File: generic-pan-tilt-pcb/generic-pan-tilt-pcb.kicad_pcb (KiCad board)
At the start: 2 copper layers, 104 x 57 mm, 86 parts, among them J1 B4P-VH-FB-B, J10 USB4115-03-C, J11 Conn_01x08, J12 Conn_01x08, J13 Conn_01x05, J2 NC5MAV, J3 NC5FAV, J5 BM03B-SRSS-TB, J7 BM03B-SRSS-TB, J8 B12B-PH-SM4-TB, J9 B12B-PH-SM4-TB, SW1 PTS 647 SK70 SMTR2 LFS, SW2 PTS 647 SK70 SMTR2 LFS, SW3 219-12LPST, U1 RP2040, U2 W25Q128JVS, U3 AP63203WU, U4 ISO1450DW, U5 MCP23017_SO, U6 LIS3DH, Y1 ABM8-272-T3

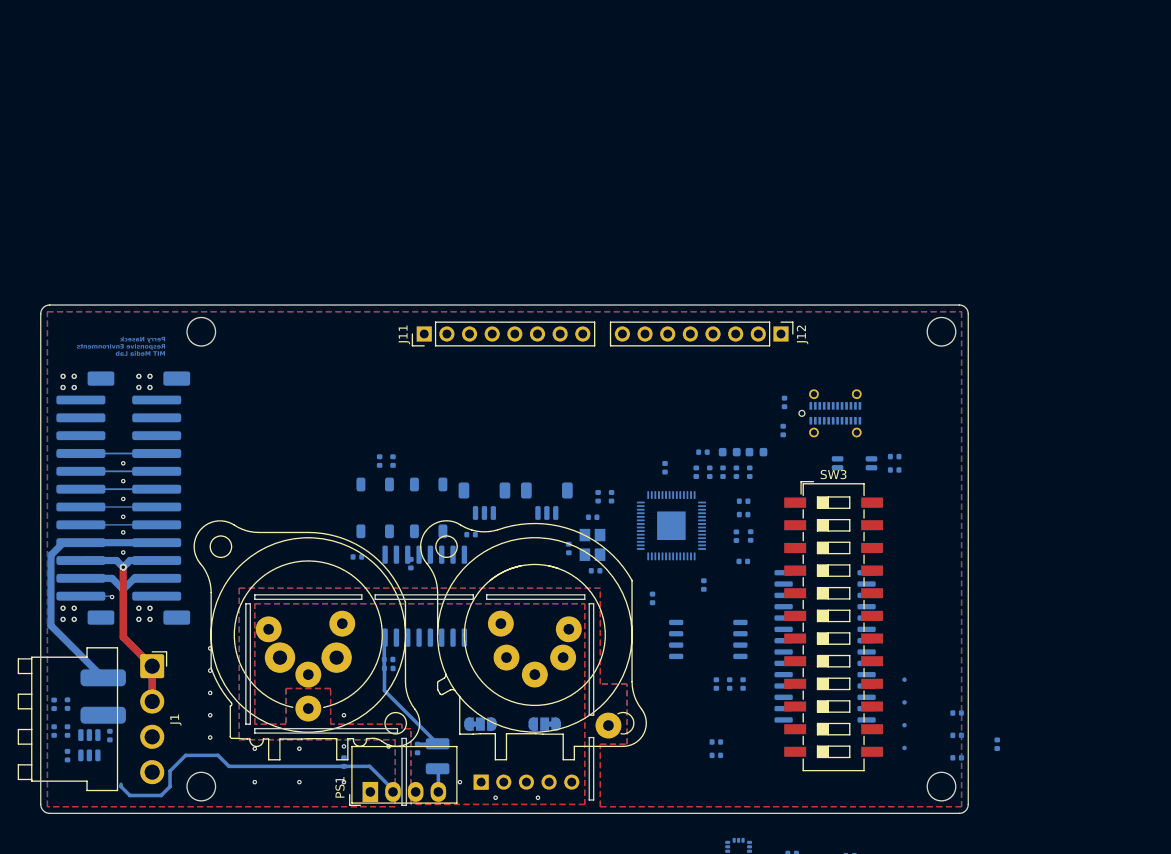
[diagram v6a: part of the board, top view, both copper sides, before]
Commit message: transplant hardware guide rp2040
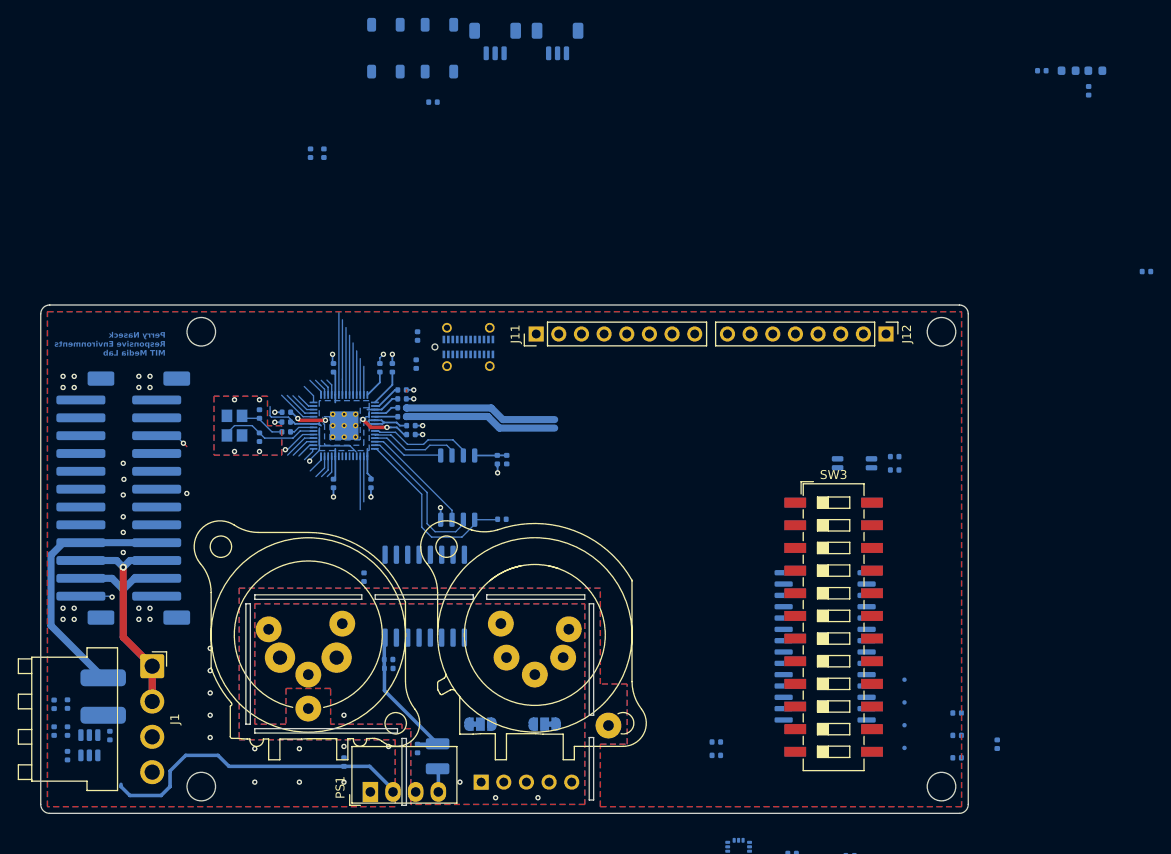
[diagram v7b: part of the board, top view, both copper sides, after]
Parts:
- removed C11: 0.1µF 10V, Capacitor_SMD:C_0402_1005Metric
- J5, J7: value BM03B-SRSS-TB -> BM03B-SRSS-TBT
- J8, J9: value B12B-PH-SM4-TB -> B12B-PH-SM4-TBT
- moved R8 81.3 mm to (205.0, 62.8)
- moved D1 57.2 mm to (196.2, 40.2)
- moved D2 57.2 mm to (199.2, 40.2)
- moved R1 57.2 mm to (193.2, 40.2)
- moved R3 57.2 mm to (198.5, 42.5)
- moved C5 53.9 mm to (108.5, 78.5), turned to 180 degrees
- moved R2 51.7 mm to (125.0, 43.8)
- moved J5 51.6 mm to (138.9, 37.0)
- moved J7 51.6 mm to (131.9, 37.0)
- moved SW1 51.6 mm to (119.7, 37.7)
- moved SW2 51.6 mm to (125.7, 37.7)
- moved Y1 42.3 mm to (102.7, 80.0)
- moved J10 41.8 mm to (128.9, 71.2)
- moved R5 41.8 mm to (123.1, 73.1)
- moved R4 41.8 mm to (123.2, 70.0)
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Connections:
- Y1 pad 1: GND -> /generic-pan-tilt-pcb_rp2040/XIN
- Y1 pad 2: /generic-pan-tilt-pcb_rp2040/XOUT_R -> GND
- Y1 pad 3: GND -> /generic-pan-tilt-pcb_rp2040/XOUT_R
- Y1 pad 4: /generic-pan-tilt-pcb_rp2040/XIN -> GND
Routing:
- net +3V3: track 66.5 -> 105.7 mm
- net /BOOTSEL: track 0.00 -> 21.2 mm
- net /USB_D-: track 0.00 -> 17.2 mm
- net /USB_D+: track 0.00 -> 17.2 mm
- net +1V1: track 0.00 -> 17.0 mm, vias 0 -> 4
- net /generic-pan-tilt-pcb_rp2040/QSPI_SD1: track 0.00 -> 16.8 mm
- net GND: track 3.54 -> 20.3 mm, vias 35 -> 53
- net /generic-pan-tilt-pcb_rp2040/QSPI_SD2: track 0.00 -> 12.9 mm
- net /generic-pan-tilt-pcb_rp2040/QSPI_SD3: track 0.00 -> 11.8 mm
- net /generic-pan-tilt-pcb_rp2040/XIN: track 0.00 -> 11.2 mm
- net /EXP_IRQ0: track 0.00 -> 10.5 mm, vias 0 -> 1
- net /generic-pan-tilt-pcb_rp2040/QSPI_CLK: track 0.00 -> 10.4 mm
- net /SPI_MOT_CS_MOT0_GPIO: track 0.00 -> 9.33 mm
- net /I2C_MOT_SDA: track 8.50 -> 0.00 mm
- net /I2C_MOT_SCL: track 8.50 -> 0.00 mm
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- added copper zone on B.Cu, net +1V1
- added copper zone on B.Cu, net +3V3

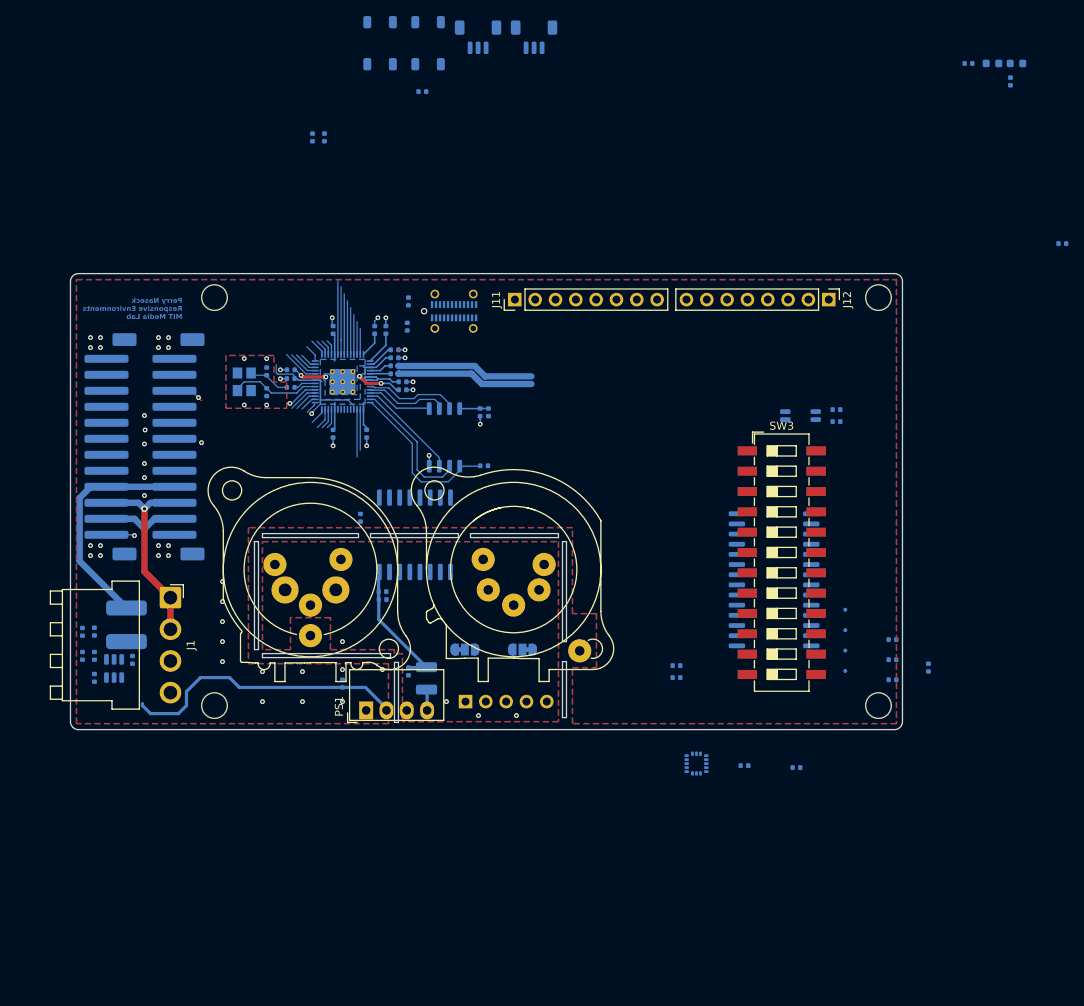
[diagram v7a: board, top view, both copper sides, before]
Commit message: mostly done with rp2040, horizontal usb
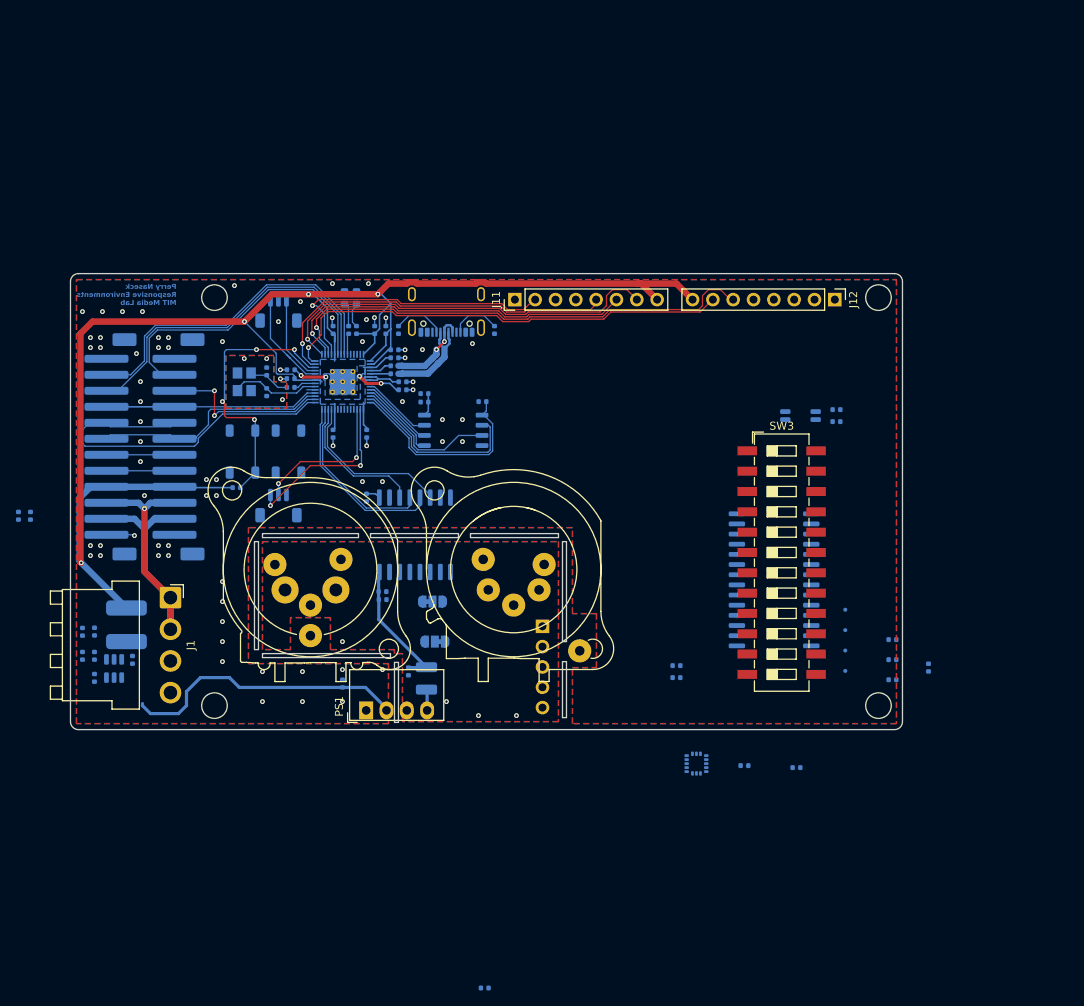
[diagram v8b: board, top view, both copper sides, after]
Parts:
- J10: value USB4115-03-C -> USB4105-GF-A; footprint Connector_USB:USB_C_Receptacle_GCT_USB4115-03-C -> Connector_USB:USB_C_Receptacle_GCT_USB4105-xx-A_16P_TopMnt_Horizontal
- moved R2 112.3 mm to (132.8, 155.8)
- moved R8 107.6 mm to (101.8, 93.2)
- moved D2 89.0 mm to (115.2, 69.5), turned to -90 degrees
- moved R3 88.4 mm to (115.8, 73.5)
- moved D1 84.7 mm to (116.8, 69.5), turned to -90 degrees
- moved R1 83.4 mm to (116.8, 73.5), turned to 90 degrees
- moved J7 63.6 mm to (107.0, 95.5), turned to 0 degrees
- moved R13 59.9 mm to (76.0, 96.8)
- moved R14 59.9 mm to (74.5, 96.8)
- moved SW2 56.1 mm to (102.5, 88.8)
- moved SW1 52.3 mm to (108.2, 88.8)
- moved J5 46.8 mm to (107.0, 71.2), turned to 0 degrees
- moved J13 13.5 mm to (140.0, 110.6), turned to 180 degrees
- moved R4 11.3 mm to (134.0, 73.5)
- moved JP1 11.0 mm to (126.5, 112.5)
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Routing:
- net +3V3: track 105.7 -> 256.5 mm, vias 0 -> 4
- net /EXP_CS1: track 1.96 -> 60.9 mm, vias 0 -> 1
- net /EXP_CS0: track 2.22 -> 57.5 mm, vias 0 -> 1
- net /EXP_SCK: track 2.16 -> 49.9 mm, vias 0 -> 1
- net /SPI_MOT_POCI: track 1.63 -> 45.8 mm
- net /EXP_POCI: track 2.14 -> 45.4 mm, vias 0 -> 1
- net /EXP_PICO: track 2.06 -> 45.1 mm, vias 0 -> 1
- net /SPI_MOT_CS_MOT1_GPIO: track 7.56 -> 42.8 mm
- net /EXP_RESET: track 1.89 -> 36.6 mm, vias 0 -> 1
- net /SPI_MOT_CS_MOT1_CNTLR: track 8.43 -> 42.9 mm
- net /SPI_MOT_CS_MOT0_GPIO: track 9.33 -> 40.6 mm
- net /RESET: track 2.95 -> 34.1 mm, vias 0 -> 4
- net /SPI_MOT_SCK: track 2.91 -> 29.8 mm
- net /SPI_MOT_PICO: track 5.24 -> 28.3 mm
- net /RS485_DE: track 2.14 -> 23.2 mm
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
